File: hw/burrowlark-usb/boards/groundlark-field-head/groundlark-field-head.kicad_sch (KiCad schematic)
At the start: 0 parts

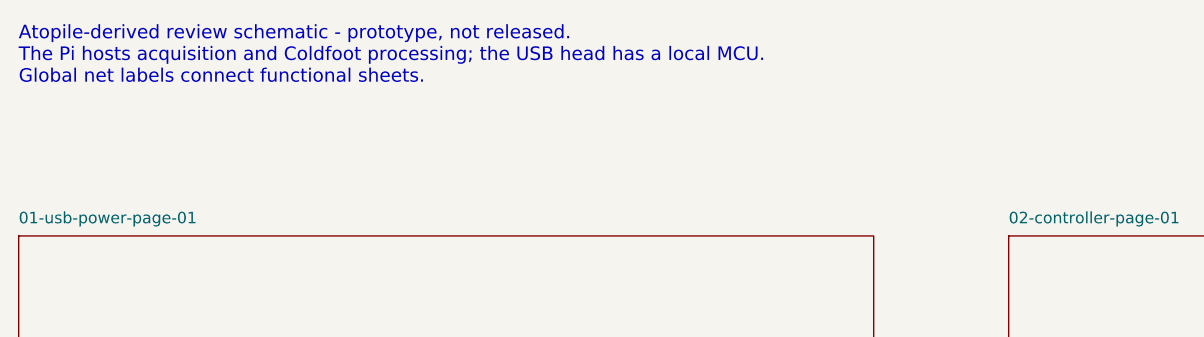
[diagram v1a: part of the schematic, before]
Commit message: Remove retired ASIC HAT variant and references
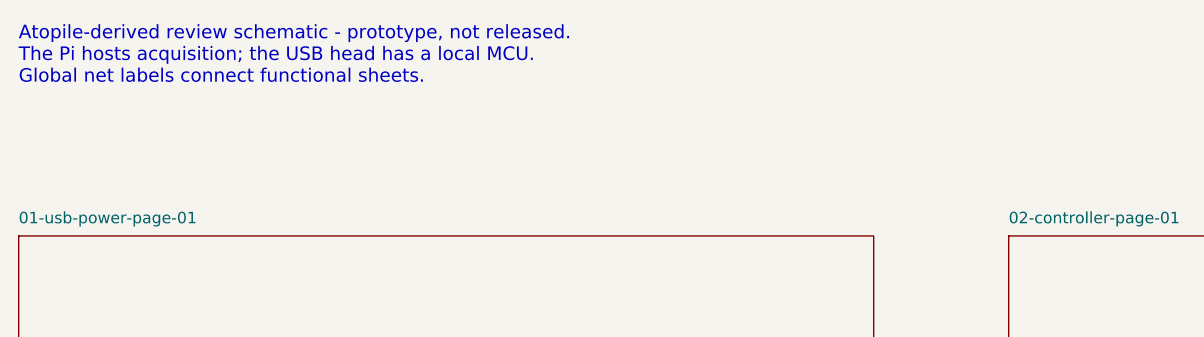
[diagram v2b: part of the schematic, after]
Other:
- note added: "Atopile-derived review schematic - prototype, not released. The Pi hosts acquisition; the USB head has a local MCU. Global net labels connect functional sheets."
- note removed: "Atopile-derived review schematic - prototype, not released. The Pi hosts acquisition and Coldfoot processing; the USB head has a local MCU. Global net labels connect functional sheets."
